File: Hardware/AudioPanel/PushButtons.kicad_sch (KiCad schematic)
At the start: 38 parts, among them CN3 4x 10nF, CN4 4x 10nF, CN5 4x 10nF, U10 74HC14, U11 74HC14, U16 MCP23017_ML

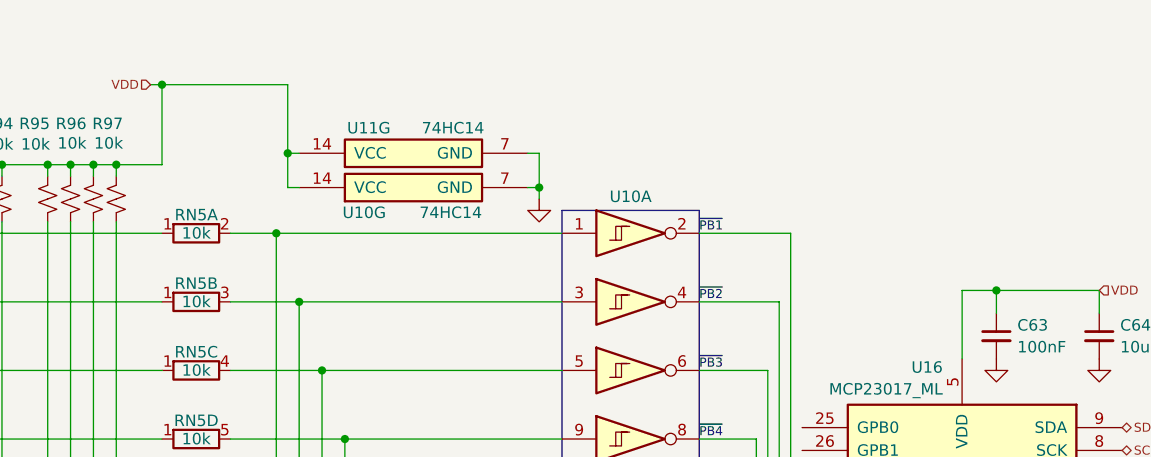
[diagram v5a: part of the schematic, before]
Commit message: Added PCM2904 audio codec
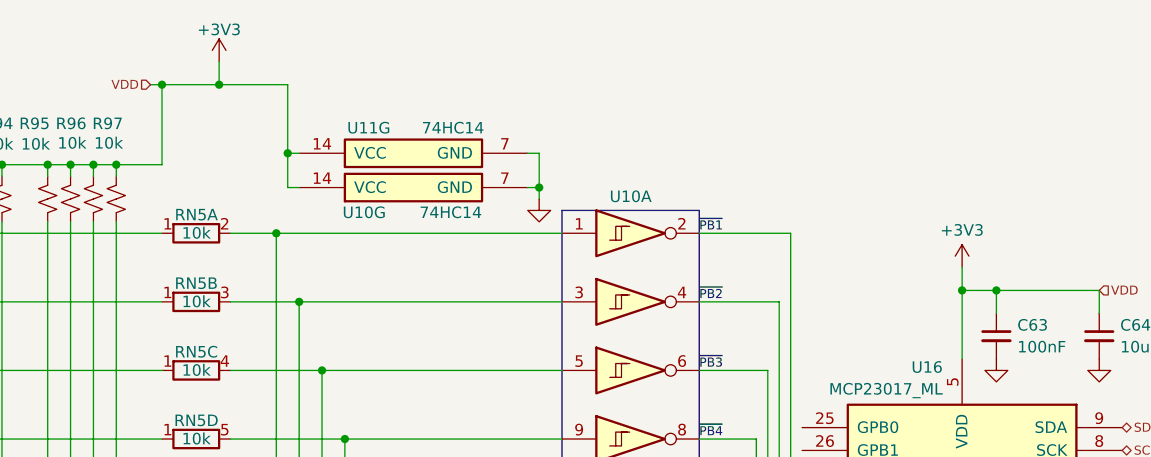
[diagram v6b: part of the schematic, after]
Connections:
- net VDD renamed +3V3
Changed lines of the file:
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@@
 	)
 	(junction
+		(at 118.11 43.18)
+		(diameter 0)
+		(color 0 0 0 0)
+	)
+	(junction
 		(at 138.43 97.79)
 		(diameter 0)
@@
 	)
 	(junction
+		(at 200.66 66.04)
+		(diameter 0)
+		(color 0 0 0 0)
+	)
+	(junction
 		(at 48.26 105.41)
 		(diameter 0)
@@
 	(wire
 		(pts
+			(xy 118.11 40.64) (xy 118.11 43.18)
+		)
+		(stroke
+			(width 0)
+			(type default)
+		)
+	)
+	(wire
+		(pts
 			(xy 81.28 58.42) (xy 81.28 82.55)
 		)
@@
 	(wire
 		(pts
+			(xy 200.66 63.5) (xy 200.66 66.04)
+		)
+		(stroke
+			(width 0)
+			(type default)
+		)
+	)
+	(wire
+		(pts
 			(xy 132.08 82.55) (xy 132.08 144.78)
 		)
@@
 	(wire
 		(pts
-			(xy 111.76 43.18) (xy 125.73 43.18)
+			(xy 118.11 43.18) (xy 111.76 43.18)
 		)
 		(stroke
@@
 	(wire
 		(pts
+			(xy 125.73 43.18) (xy 118.11 43.18)
+		)
+		(stroke
+			(width 0)
+			(type default)
+		)
+	)
+	(wire
+		(pts
 			(xy 78.74 58.42) (xy 78.74 74.93)
 		)
@@
 	)
 	(symbol
+		(lib_id "power:+3V3")
+		(at 200.66 63.5 0)
+		(unit 1)
+		(exclude_from_sim no)
+		(in_bom yes)
+		(on_board yes)
+		(dnp no)
+		(fields_autoplaced yes)
+		(property "Reference" "#PWR0114"
+			(at 200.66 67.31 0)
+			(effects
+				(font
+					(size 1.27 1.27)
+				)
+				(hide yes)
+			)
+		)
+		(property "Value" "+3V3"
+			(at 200.66 59.3669 0)
+			(effects
+				(font
+					(size 1.27 1.27)
+				)
+			)
+		)
+		(property "Footprint" ""
+			(at 200.66 63.5 0)
+			(effects
+				(font
+					(size 1.27 1.27)
+				)
+				(hide yes)
+			)
+		)
+		(property "Datasheet" ""
+			(at 200.66 63.5 0)
+			(effects
+				(font
+					(size 1.27 1.27)
+				)
+				(hide yes)
+			)
+		)
+		(property "Description" "Power symbol creates a global label with name \"+3V3\""
+			(at 200.66 63.5 0)
+			(effects
+				(font
+					(size 1.27 1.27)
+				)
+				(hide yes)
+			)
+		)
+		(pin "1"
+		)
+		(instances
+			(project "PilotAudioPanel"
+				(path "/2de36a1b-eee5-458c-8325-256a7162eff5/a5cce8a2-fa1f-45df-8605-c295d18be7f1/292d3d4d-f17c-45e8-bc8b-f5444b88eee7"
+					(reference "#PWR0114")
+					(unit 1)
+				)
+			)
+		)
+	)
+	(symbol
 		(lib_id "Power_Protection:SP0504BAJT")
 		(at 101.6 149.86 0)
@@
 					(unit 1)
 				)
+			)
+		)
+	)
+	(symbol
+		(lib_id "power:+3V3")
+		(at 118.11 40.64 0)
+		(unit 1)
+		(exclude_from_sim no)
+		(in_bom yes)
+		(on_board yes)
+		(dnp no)
+		(property "Reference" "#PWR054"
+			(at 118.11 44.45 0)
+			(effects
+				(font
+					(size 1.27 1.27)
+				)
+				(hide yes)
+			)
+		)
+		(property "Value" "+3V3"
+			(at 118.11 37.084 0)
+			(effects
+				(font
+					(size 1.27 1.27)
+				)
+			)
+		)
+		(property "Footprint" ""
+			(at 118.11 40.64 0)
+			(effects
+				(font
+					(size 1.27 1.27)
+				)
+				(hide yes)
+			)
+		)
+		(property "Datasheet" ""
+			(at 118.11 40.64 0)
+			(effects
+				(font
+					(size 1.27 1.27)
+				)
+				(hide yes)
+			)
+		)
+		(property "Description" "Power symbol creates a global label with name \"+3V3\""
+			(at 118.11 40.64 0)
+			(effects
+				(font
+					(size 1.27 1.27)
+				)
+				(hide yes)
+			)
+		)
+		(pin "1"
+		)
+		(instances
+			(project "PilotAudioPanel"
+				(path "/2de36a1b-eee5-458c-8325-256a7162eff5/a5cce8a2-fa1f-45df-8605-c295d18be7f1/292d3d4d-f17c-45e8-bc8b-f5444b88eee7"
+					(reference "#PWR054")
+					(unit 1)
+				)
